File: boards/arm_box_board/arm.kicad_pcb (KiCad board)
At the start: 2 copper layers, 14 parts

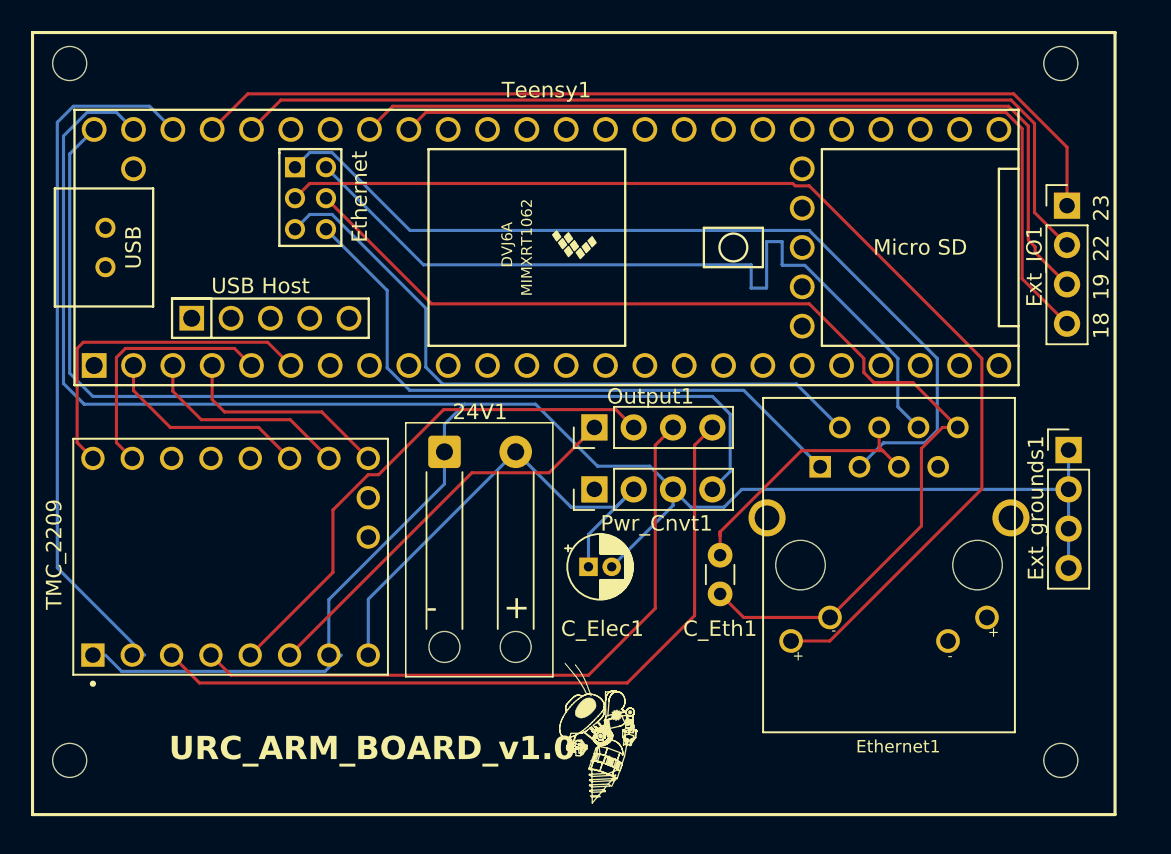
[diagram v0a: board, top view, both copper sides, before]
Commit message: Changes to Science and Arm Board
Added pin labels to both boards
Fixed Mislabeled Stepper Board Footprint in Arm board
Added extra digital pins and ground in Science Board
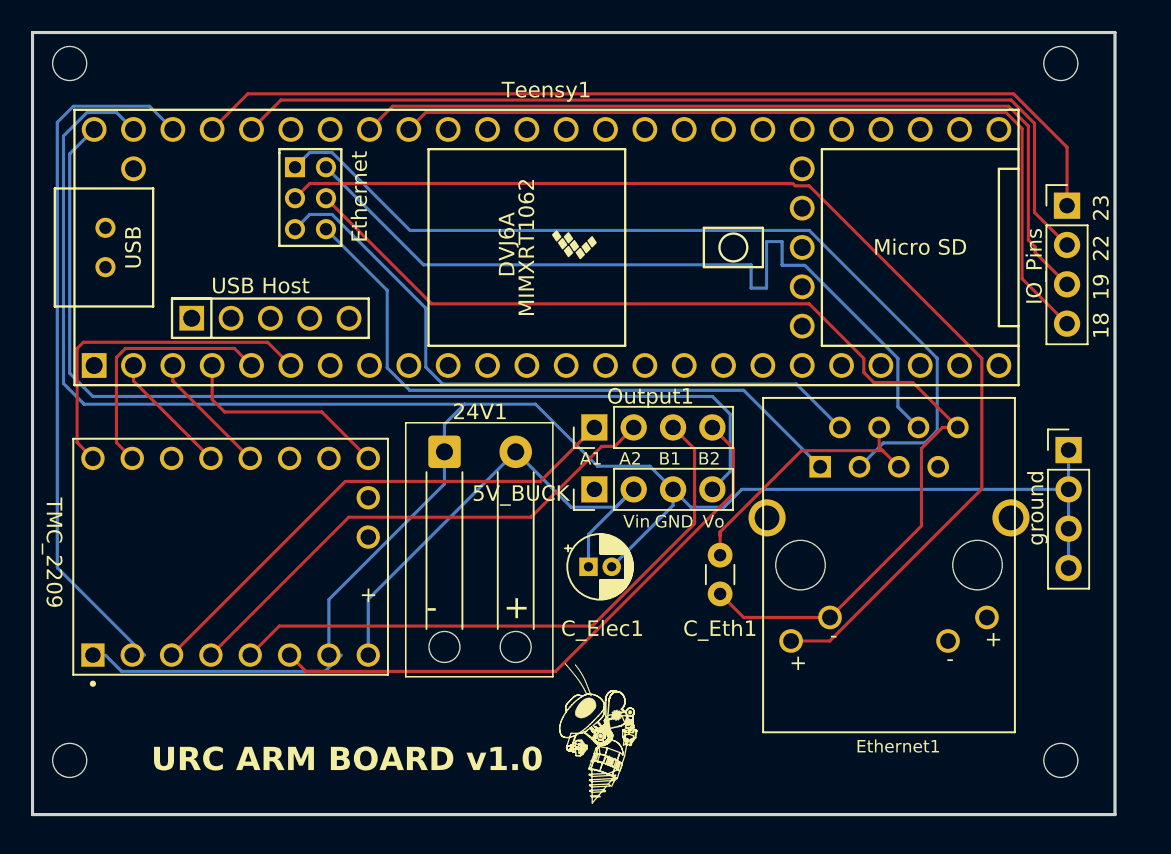
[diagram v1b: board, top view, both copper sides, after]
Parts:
- renumbered Pwr_Cnvt1 to 5V_BUCK, Ext_IO1 to IO_Pins, Ext_grounds1 to ground
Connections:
- Output1 pad 1: Net-(Output1-Pin_1) -> /A1
- Output1 pad 2: Net-(Output1-Pin_2) -> /A2
- Output1 pad 3: Net-(Output1-Pin_3) -> /B1
- Output1 pad 4: Net-(Output1-Pin_4) -> /B2
- TMC_2209 pad 12: unconnected-(TMC_2209-UART-Pad12) -> Net-(TMC_2209-TX)
- TMC_2209 pad 13: unconnected-(TMC_2209-SPRD-Pad13) -> Net-(TMC_2209-RX)
- TMC_2209 pad 14: Net-(TMC_2209-MS2) -> unconnected-(TMC_2209-MS2-Pad14)
- TMC_2209 pad 15: Net-(TMC_2209-MS1) -> unconnected-(TMC_2209-MS1-Pad15)
- TMC_2209 pad 3: Net-(Output1-Pin_4) -> /A1
- TMC_2209 pad 4: Net-(Output1-Pin_3) -> /A2
- TMC_2209 pad 5: Net-(Output1-Pin_2) -> /B1
- TMC_2209 pad 6: Net-(Output1-Pin_1) -> /B2
- Teensy1 pad 2: Net-(TMC_2209-MS2) -> Net-(TMC_2209-TX)
- Teensy1 pad 3: Net-(TMC_2209-MS1) -> Net-(TMC_2209-RX)
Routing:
- net Net-(Output1-Pin_4): track 48.9 -> 0.00 mm
- net Net-(Output1-Pin_3): track 43.2 -> 0.00 mm
- net /B2: track 0.00 -> 39.2 mm
- net /B1: track 0.00 -> 39.0 mm
- net Net-(Output1-Pin_2): track 34.2 -> 0.00 mm
- net /A2: track 0.00 -> 33.4 mm
- net /A1: track 0.00 -> 33.4 mm
- net Net-(Output1-Pin_1): track 25.8 -> 0.00 mm
- net Net-(TMC_2209-MS1): track 13.5 -> 0.00 mm
- net Net-(TMC_2209-MS2): track 13.5 -> 0.00 mm
- net Net-(TMC_2209-TX): track 0.00 -> 8.07 mm
- net Net-(TMC_2209-RX): track 0.00 -> 8.07 mm
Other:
- board outline added: 69.9 x 50.5 mm
- board text added: "A1"
- board text added: "A2"
- board text added: "B1"
- board text added: "B2"
- board text added: "GND"
- board text added: "TMC_2209"
- board text added: "URC ARM BOARD v1.0"
- board text added: "Vin"
- board text added: "Vo"
- board text removed: "URC_ARM_BOARD_v1.0"

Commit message: Prepared Boards for PCB Manufacture
Added GND line for IMU on Main Board
Fixed Silkscreen Text Size for PCB Manufacture on Science, Main, and Arm boards
Generated Gerber Files for Science, Main, and Arm boards
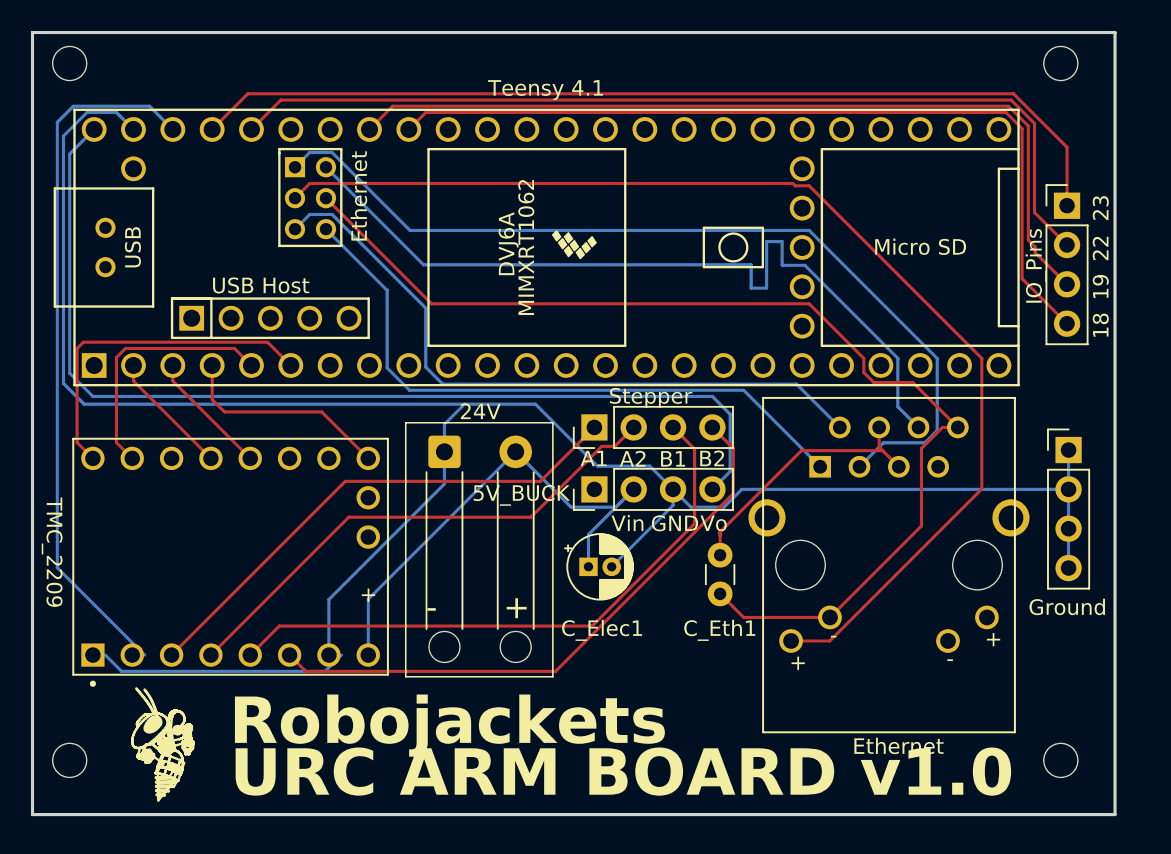
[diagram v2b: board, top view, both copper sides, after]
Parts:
- Teensy 4.1: renamed from Teensy1
- renumbered 24V1 to 24V, Ethernet1 to Ethernet, ground to Ground, Output1 to Stepper
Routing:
- net Net-(Ethernet1-GND): track 72.0 -> 71.5 mm
- net /B2: track 39.2 -> 38.7 mm
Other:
- board text added: "Robojackets"
